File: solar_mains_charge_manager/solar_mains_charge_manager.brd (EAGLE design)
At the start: 100 x 80 mm, 26 parts, among them T1 TIP122, X1 22-23-2031, X2 22-23-2021, X3 22-23-2031, X4 22-23-2031, X5 22-23-2031, X6 22-23-2041, X7 53047-15, X8 53047-15

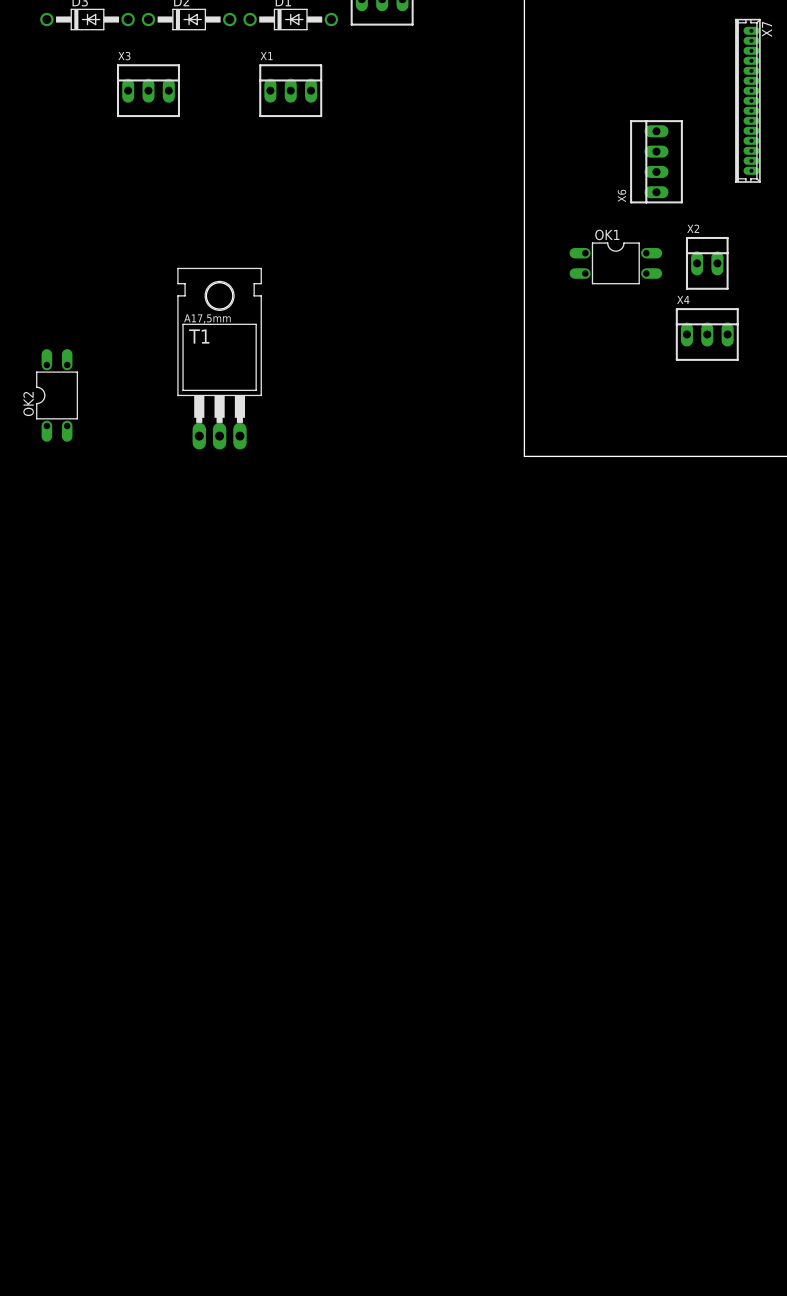
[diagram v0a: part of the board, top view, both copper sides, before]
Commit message: Added solar panel voltage measurement along with over voltage and negative voltage protection in schematic, plus comments on the same in psu_considerations.ods
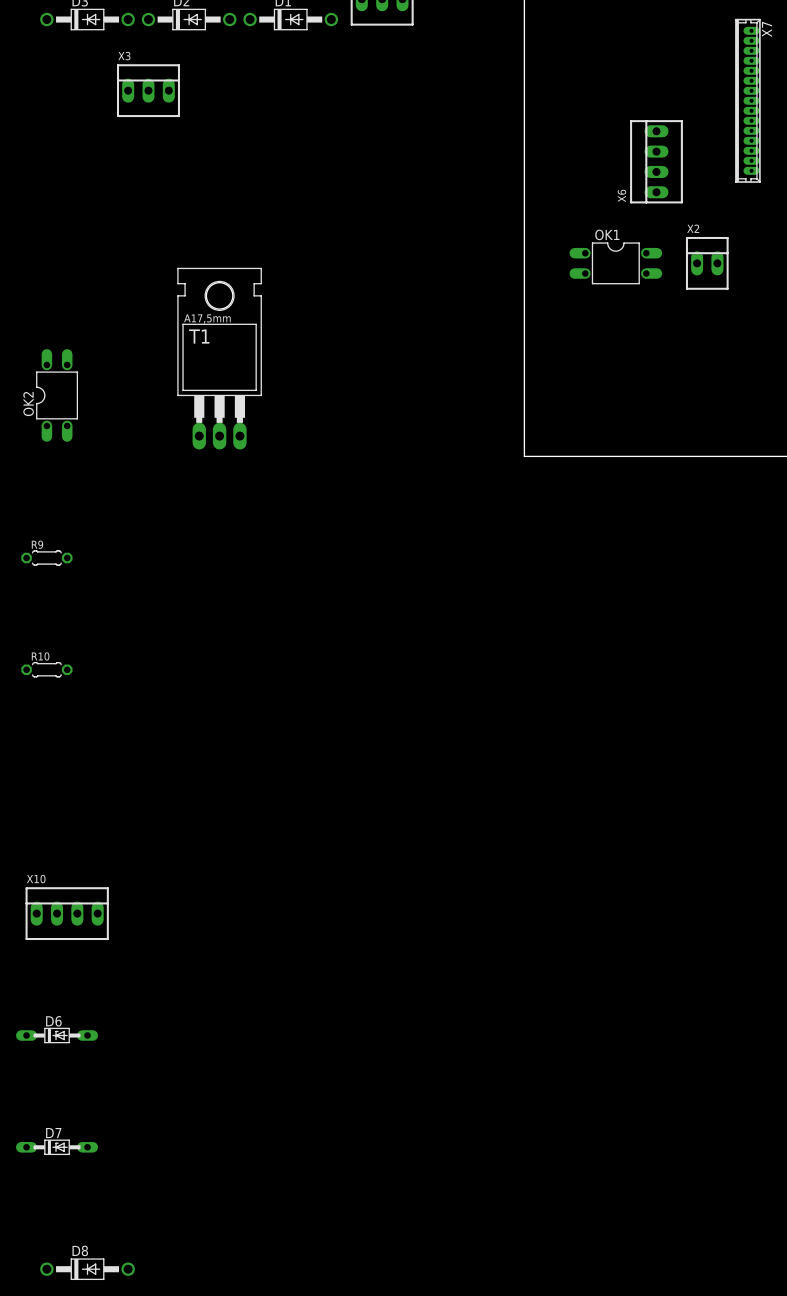
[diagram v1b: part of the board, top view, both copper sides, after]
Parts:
- removed X1, X4: 22-23-2031, con-molex:22-23-2031
- added D6, D7: (no value), diode:DO34Z7
- added D8: 1N4004, diode:DO41-10
- added R10, R9: (no value), resistor:0204/5
- added X10: 22-23-2041, con-molex:22-23-2041
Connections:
- new net N$41: R10.1, X10.4
- new net N$42: R9.1, X10.3
- net 12V: now also X5.3; no longer X4.2
- net BAT: now also X10.2; no longer X1.2
- net GND: now also D6.A, D7.A, D8.A, X10.1; no longer X1.1, X4.1
- net N$3: now also D6.C
- net N$39: now also D7.C, D8.C, R10.2, R9.2
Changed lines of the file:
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@@
 <element name="T1" library="transistor" library_urn="urn:adsk.eagle:library:402" package="TO220" package3d_urn="urn:adsk.eagle:package:29897/1" value="TIP122" x="-38.1" y="8.89"/>
 <element name="U$1" library="Arduino-clone" package="NANO" value="NANO" x="48.26" y="34.29"/>
-<element name="X1" library="con-molex" library_urn="urn:adsk.eagle:library:165" package="22-23-2031" value="22-23-2031" x="-29.21" y="45.72">
-<attribute name="MF" value="MOLEX" x="-29.21" y="45.72" size="1.778" layer="27" display="off"/>
-<attribute name="MPN" value="22-23-2031" x="-29.21" y="45.72" size="1.778" layer="27" display="off"/>
-<attribute name="OC_FARNELL" value="1462950" x="-29.21" y="45.72" size="1.778" layer="27" display="off"/>
-<attribute name="OC_NEWARK" value="30C0862" x="-29.21" y="45.72" size="1.778" layer="27" display="off"/>
-</element>
 <element name="X2" library="con-molex" library_urn="urn:adsk.eagle:library:165" package="22-23-2021" value="22-23-2021" x="22.86" y="24.13">
 <attribute name="MF" value="MOLEX" x="22.86" y="24.13" size="1.778" layer="27" display="off"/>
@@
 <attribute name="OC_NEWARK" value="30C0862" x="-46.99" y="45.72" size="1.778" layer="27" display="off"/>
 </element>
-<element name="X4" library="con-molex" library_urn="urn:adsk.eagle:library:165" package="22-23-2031" value="22-23-2031" x="22.86" y="15.24">
-<attribute name="MF" value="MOLEX" x="22.86" y="15.24" size="1.778" layer="27" display="off"/>
-<attribute name="MPN" value="22-23-2031" x="22.86" y="15.24" size="1.778" layer="27" display="off"/>
-<attribute name="OC_FARNELL" value="1462950" x="22.86" y="15.24" size="1.778" layer="27" display="off"/>
-<attribute name="OC_NEWARK" value="30C0862" x="22.86" y="15.24" size="1.778" layer="27" display="off"/>
-</element>
 <element name="X5" library="con-molex" library_urn="urn:adsk.eagle:library:165" package="22-23-2031" value="22-23-2031" x="-17.78" y="57.15">
 <attribute name="MF" value="MOLEX" x="-17.78" y="57.15" size="1.778" layer="27" display="off"/>
@@
 <attribute name="OC_NEWARK" value="79K4146" x="62.23" y="44.45" size="1.778" layer="27" rot="R90" display="off"/>
 </element>
+<element name="R9" library="resistor" library_urn="urn:adsk.eagle:library:348" package="0204/5" package3d_urn="urn:adsk.eagle:package:25955/1" value="" x="-59.69" y="-12.7"/>
+<element name="R10" library="resistor" library_urn="urn:adsk.eagle:library:348" package="0204/5" package3d_urn="urn:adsk.eagle:package:25955/1" value="" x="-59.69" y="-26.67"/>
+<element name="X10" library="con-molex" library_urn="urn:adsk.eagle:library:165" package="22-23-2041" value="22-23-2041" x="-57.15" y="-57.15">
+<attribute name="MF" value="MOLEX" x="-57.15" y="-57.15" size="1.778" layer="27" display="off"/>
+<attribute name="MPN" value="22-23-2041" x="-57.15" y="-57.15" size="1.778" layer="27" display="off"/>
+<attribute name="OC_FARNELL" value="1462920" x="-57.15" y="-57.15" size="1.778" layer="27" display="off"/>
+<attribute name="OC_NEWARK" value="38C0355" x="-57.15" y="-57.15" size="1.778" layer="27" display="off"/>
+</element>
+<element name="D6" library="diode" library_urn="urn:adsk.eagle:library:210" package="DO34Z7" package3d_urn="urn:adsk.eagle:package:43364/1" value="" x="-58.42" y="-72.39"/>
+<element name="D7" library="diode" library_urn="urn:adsk.eagle:library:210" package="DO34Z7" package3d_urn="urn:adsk.eagle:package:43364/1" value="" x="-58.42" y="-86.36"/>
+<element name="D8" library="diode" library_urn="urn:adsk.eagle:library:210" package="DO41-10" package3d_urn="urn:adsk.eagle:package:43336/1" value="1N4004" x="-54.61" y="-101.6"/>
 </elements>
 <signals>
@@
 <contactref element="U$1" pad="A0"/>
 <contactref element="X7" pad="12"/>
-<wire x1="28.39" y1="49.45" x2="38.1" y2="53.34" width="0" layer="19" extent="1-1"/>
+<contactref element="D6" pad="C"/>
+<wire x1="28.39" y1="49.45" x2="-62.23" y2="-72.39" width="0" layer="19" extent="1-1"/>
+<wire x1="38.1" y1="53.34" x2="28.39" y2="49.45" width="0" layer="19" extent="1-1"/>
 <wire x1="-13.97" y1="76.2" x2="28.39" y2="49.45" width="0" layer="19" extent="1-1"/>
 <wire x1="-21.59" y1="76.2" x2="-13.97" y2="76.2" width="0" layer="19" extent="1-1"/>
@@
 <contactref element="X7" pad="2"/>
 <contactref element="OK1" pad="2"/>
-<contactref element="X1" pad="1"/>
 <contactref element="X5" pad="1"/>
-<contactref element="X4" pad="1"/>
 <contactref element="T1" pad="3"/>
 <contactref element="OK2" pad="3"/>
 <contactref element="X3" pad="1"/>
 <contactref element="X6" pad="1"/>
-<wire x1="28.39" y1="36.95" x2="38.1" y2="27.94" width="0" layer="19" extent="1-1"/>
-<wire x1="16.51" y1="33.02" x2="28.39" y2="36.95" width="0" layer="19" extent="1-1"/>
+<contactref element="X10" pad="1"/>
+<contactref element="D6" pad="A"/>
+<contactref element="D7" pad="A"/>
+<contactref element="D8" pad="A"/>
+<wire x1="-54.61" y1="-86.36" x2="-49.53" y2="-101.6" width="0" layer="19" extent="1-1"/>
+<wire x1="-54.61" y1="-72.39" x2="-54.61" y2="-86.36" width="0" layer="19" extent="1-1"/>
+<wire x1="-60.96" y1="-57.15" x2="-54.61" y2="-72.39" width="0" layer="19" extent="1-1"/>
+<wire x1="-35.56" y1="2.54" x2="-60.96" y2="-57.15" width="0" layer="19" extent="1-1"/>
+<wire x1="-57.15" y1="11.43" x2="-35.56" y2="2.54" width="0" layer="19" extent="1-1"/>
+<wire x1="-49.53" y1="45.72" x2="-57.15" y2="11.43" width="0" layer="19" extent="1-1"/>
+<wire x1="-20.32" y1="57.15" x2="-49.53" y2="45.72" width="0" layer="19" extent="1-1"/>
+<wire x1="-26.67" y1="76.2" x2="-20.32" y2="57.15" width="0" layer="19" extent="1-1"/>
+<wire x1="16.51" y1="33.02" x2="-20.32" y2="57.15" width="0" layer="19" extent="1-1"/>
+<wire x1="28.39" y1="36.95" x2="16.51" y2="33.02" width="0" layer="19" extent="1-1"/>
+<wire x1="38.1" y1="27.94" x2="28.39" y2="36.95" width="0" layer="19" extent="1-1"/>
 <wire x1="7.62" y1="22.86" x2="16.51" y2="33.02" width="0" layer="19" extent="1-1"/>
-<wire x1="20.32" y1="15.24" x2="7.62" y2="22.86" width="0" layer="19" extent="1-1"/>
-<wire x1="-20.32" y1="57.15" x2="16.51" y2="33.02" width="0" layer="19" extent="1-1"/>
-<wire x1="-31.75" y1="45.72" x2="-20.32" y2="57.15" width="0" layer="19" extent="1-1"/>
-<wire x1="-49.53" y1="45.72" x2="-31.75" y2="45.72" width="0" layer="19" extent="1-1"/>
-<wire x1="-26.67" y1="76.2" x2="-20.32" y2="57.15" width="0" layer="19" extent="1-1"/>
-<wire x1="-57.15" y1="11.43" x2="-49.53" y2="45.72" width="0" layer="19" extent="1-1"/>
-<wire x1="-35.56" y1="2.54" x2="-57.15" y2="11.43" width="0" layer="19" extent="1-1"/>
 </signal>
 <signal name="N$2">
@@
 <contactref element="U$1" pad="RAW"/>
 <contactref element="X7" pad="1"/>
-<contactref element="X4" pad="2"/>
 <contactref element="X2" pad="1"/>
 <contactref element="OK1" pad="4"/>
+<contactref element="X5" pad="3"/>
 <wire x1="28.39" y1="35.7" x2="38.1" y2="25.4" width="0" layer="19" extent="1-1"/>
 <wire x1="21.59" y1="24.13" x2="28.39" y2="35.7" width="0" layer="19" extent="1-1"/>
 <wire x1="15.24" y1="25.4" x2="21.59" y2="24.13" width="0" layer="19" extent="1-1"/>
-<wire x1="22.86" y1="15.24" x2="21.59" y2="24.13" width="0" layer="19" extent="1-1"/>
+<wire x1="-15.24" y1="57.15" x2="15.24" y2="25.4" width="0" layer="19" extent="1-1"/>
 </signal>
 <signal name="BAT">
 <contactref element="R1" pad="1"/>
-<contactref element="X1" pad="2"/>
 <contactref element="X5" pad="2"/>
-<wire x1="-17.78" y1="57.15" x2="-19.05" y2="76.2" width="0" layer="19" extent="1-1"/>
-<wire x1="-29.21" y1="45.72" x2="-17.78" y2="57.15" width="0" layer="19" extent="1-1"/>
+<contactref element="X10" pad="2"/>
+<wire x1="-17.78" y1="57.15" x2="-58.42" y2="-57.15" width="0" layer="19" extent="1-1"/>
+<wire x1="-19.05" y1="76.2" x2="-17.78" y2="57.15" width="0" layer="19" extent="1-1"/>
 </signal>
 <signal name="N$5">
@@
 <contactref element="X7" pad="11"/>
 <contactref element="U$1" pad="A1"/>
-<wire x1="28.39" y1="48.2" x2="38.1" y2="50.8" width="0" layer="19" extent="1-1"/>
+<contactref element="R9" pad="2"/>
+<contactref element="R10" pad="2"/>
+<contactref element="D7" pad="C"/>
+<contactref element="D8" pad="C"/>
+<wire x1="-62.23" y1="-86.36" x2="-59.69" y2="-101.6" width="0" layer="19" extent="1-1"/>
+<wire x1="-57.15" y1="-26.67" x2="-62.23" y2="-86.36" width="0" layer="19" extent="1-1"/>
+<wire x1="-57.15" y1="-12.7" x2="-57.15" y2="-26.67" width="0" layer="19" extent="1-1"/>
+<wire x1="28.39" y1="48.2" x2="-57.15" y2="-12.7" width="0" layer="19" extent="1-1"/>
+<wire x1="38.1" y1="50.8" x2="28.39" y2="48.2" width="0" layer="19" extent="1-1"/>
+</signal>
+<signal name="N$41">
+<contactref element="X10" pad="4"/>
+<contactref element="R10" pad="1"/>
+<wire x1="-62.23" y1="-26.67" x2="-53.34" y2="-57.15" width="0" layer="19" extent="1-1"/>
+</signal>
+<signal name="N$42">
+<contactref element="X10" pad="3"/>
+<contactref element="R9" pad="1"/>
+<wire x1="-62.23" y1="-12.7" x2="-55.88" y2="-57.15" width="0" layer="19" extent="1-1"/>
 </signal>
 </signals>

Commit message: Continued work on adding overvoltage protection on analog inputs and measurement of solar panel voltage
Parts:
- added R11, R12: (no value), resistor:0204/5
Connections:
- new net N$40: D6.C, R11.2, U$1.A0, X7.12
- new net N$43: R1.2, R11.1, R2.2
- net N$3: now also R10.2, R12.1, R9.2; no longer D6.C, R1.2, R2.2, U$1.A0, X7.12
- net N$39: now also R12.2; no longer R10.2, R9.2
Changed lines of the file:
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@@
 <element name="D7" library="diode" library_urn="urn:adsk.eagle:library:210" package="DO34Z7" package3d_urn="urn:adsk.eagle:package:43364/1" value="" x="-58.42" y="-86.36"/>
 <element name="D8" library="diode" library_urn="urn:adsk.eagle:library:210" package="DO41-10" package3d_urn="urn:adsk.eagle:package:43336/1" value="1N4004" x="-54.61" y="-101.6"/>
+<element name="R11" library="resistor" library_urn="urn:adsk.eagle:library:348" package="0204/5" package3d_urn="urn:adsk.eagle:package:25955/1" value="" x="-59.69" y="-116.84"/>
+<element name="R12" library="resistor" library_urn="urn:adsk.eagle:library:348" package="0204/5" package3d_urn="urn:adsk.eagle:package:25955/1" value="" x="-59.69" y="-130.81"/>
 </elements>
 <signals>
@@
 <wire x1="28.39" y1="51.95" x2="38.1" y2="55.88" width="0" layer="19" extent="1-1"/>
 <wire x1="28.39" y1="50.7" x2="28.39" y2="51.95" width="0" layer="19" extent="1-1"/>
-</signal>
-<signal name="N$3">
-<contactref element="R2" pad="2"/>
-<contactref element="R1" pad="2"/>
-<contactref element="U$1" pad="A0"/>
-<contactref element="X7" pad="12"/>
-<contactref element="D6" pad="C"/>
-<wire x1="28.39" y1="49.45" x2="-62.23" y2="-72.39" width="0" layer="19" extent="1-1"/>
-<wire x1="38.1" y1="53.34" x2="28.39" y2="49.45" width="0" layer="19" extent="1-1"/>
-<wire x1="-13.97" y1="76.2" x2="28.39" y2="49.45" width="0" layer="19" extent="1-1"/>
-<wire x1="-21.59" y1="76.2" x2="-13.97" y2="76.2" width="0" layer="19" extent="1-1"/>
 </signal>
 <signal name="GND">
@@
 <contactref element="X7" pad="11"/>
 <contactref element="U$1" pad="A1"/>
-<contactref element="R9" pad="2"/>
-<contactref element="R10" pad="2"/>
 <contactref element="D7" pad="C"/>
 <contactref element="D8" pad="C"/>
+<contactref element="R12" pad="2"/>
+<wire x1="-59.69" y1="-101.6" x2="-57.15" y2="-130.81" width="0" layer="19" extent="1-1"/>
 <wire x1="-62.23" y1="-86.36" x2="-59.69" y2="-101.6" width="0" layer="19" extent="1-1"/>
-<wire x1="-57.15" y1="-26.67" x2="-62.23" y2="-86.36" width="0" layer="19" extent="1-1"/>
-<wire x1="-57.15" y1="-12.7" x2="-57.15" y2="-26.67" width="0" layer="19" extent="1-1"/>
-<wire x1="28.39" y1="48.2" x2="-57.15" y2="-12.7" width="0" layer="19" extent="1-1"/>
+<wire x1="28.39" y1="48.2" x2="-62.23" y2="-86.36" width="0" layer="19" extent="1-1"/>
 <wire x1="38.1" y1="50.8" x2="28.39" y2="48.2" width="0" layer="19" extent="1-1"/>
 </signal>
@@
 <wire x1="-62.23" y1="-12.7" x2="-55.88" y2="-57.15" width="0" layer="19" extent="1-1"/>
 </signal>
+<signal name="N$40">
+<contactref element="D6" pad="C"/>
+<contactref element="R11" pad="2"/>
+<contactref element="U$1" pad="A0"/>
+<contactref element="X7" pad="12"/>
+<wire x1="-62.23" y1="-72.39" x2="-57.15" y2="-116.84" width="0" layer="19" extent="1-1"/>
+<wire x1="28.39" y1="49.45" x2="-62.23" y2="-72.39" width="0" layer="19" extent="1-1"/>
+<wire x1="38.1" y1="53.34" x2="28.39" y2="49.45" width="0" layer="19" extent="1-1"/>
+</signal>
+<signal name="N$43">
+<contactref element="R2" pad="2"/>
+<contactref element="R1" pad="2"/>
+<contactref element="R11" pad="1"/>
+<wire x1="-21.59" y1="76.2" x2="-62.23" y2="-116.84" width="0" layer="19" extent="1-1"/>
+<wire x1="-13.97" y1="76.2" x2="-21.59" y2="76.2" width="0" layer="19" extent="1-1"/>
+</signal>
+<signal name="N$3">
+<contactref element="R9" pad="2"/>
+<contactref element="R10" pad="2"/>
+<contactref element="R12" pad="1"/>
+<wire x1="-57.15" y1="-26.67" x2="-62.23" y2="-130.81" width="0" layer="19" extent="1-1"/>
+<wire x1="-57.15" y1="-12.7" x2="-57.15" y2="-26.67" width="0" layer="19" extent="1-1"/>
+</signal>
 </signals>

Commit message: A lot of stuff
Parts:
- removed C1: (no value), capacitor-wima:C5B2.5
- removed D1, D2, D3, D4, D8: 1N4004, diode:DO41-10
- removed D5, D6, D7: (no value), diode:DO34Z7
- removed OK1, OK2: PC817, optocoupler:DIL04
- removed R1, R10, R11, R12, R2, R3, R4, R5, R9: (no value), resistor:0204/5
- removed R6, R7, R8: (no value), resistor:0204/7
- removed T1: TIP122, transistor:TO220
- moved X2 28.0 mm to (21.6, 52.1), turned to 90 degrees
- moved X7 8.13 mm to (33.0, 50.8)
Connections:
- removed net N$1: U$1.3.3V, U$1.AREF, X7.13, X7.14
- removed net N$10: D3.A, D4.A, D5.A, OK2.2
- removed net N$11: D1.C, D2.C, R7.2
- removed net N$13: C1.1, D1.A, D3.C, R8.1
- removed net N$14: C1.2, R8.2
- removed net N$15: D2.A, D4.C, R6.1
- removed net N$16: R6.2
- removed net N$3: R10.2, R12.1, R9.2
- removed net N$4: OK1.1, R3.1
- removed net N$43: R1.2, R11.1, R2.2
- removed net N$6: OK1.3, R4.1
- removed net N$7: R4.2, T1.1
- removed net N$8: OK2.1, R5.1
- removed net N$9: D5.C, R5.2, R7.1
- new net 12V1: U$1.AREF, X2.1, X7.13
- net 12V: no longer OK1.4, X2.1
- net BAT: no longer R1.1
- net GND: no longer D6.A, D7.A, D8.A, OK1.2, OK2.3, R2.1, T1.3
- net N$12: no longer OK2.4
- net N$2: no longer R3.2
- net N$39: no longer D7.C, D8.C, R12.2
- net N$40: no longer D6.C, R11.2
- net N$41: no longer R10.1
- net N$42: no longer R9.1
- net N$5: now also U$1.3.3V, X7.14; no longer T1.2
